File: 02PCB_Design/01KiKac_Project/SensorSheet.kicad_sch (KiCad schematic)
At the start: 10 parts, among them J1 MTSW-104-22-L-D-265-RA, U1 AS5047P-ATSM, U2 ISM330BXTR

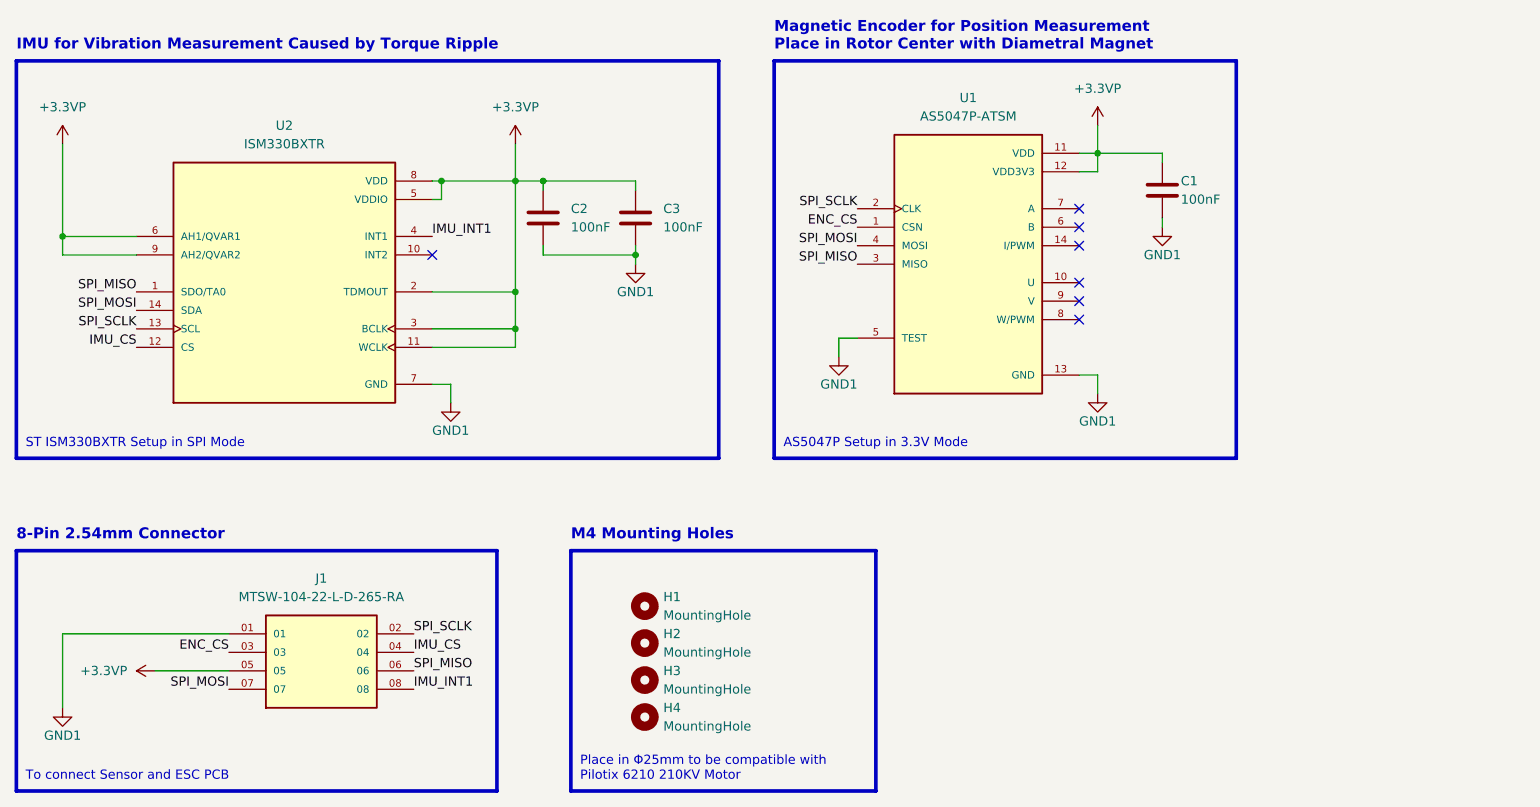
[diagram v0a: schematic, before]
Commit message: added CAN + minor changes
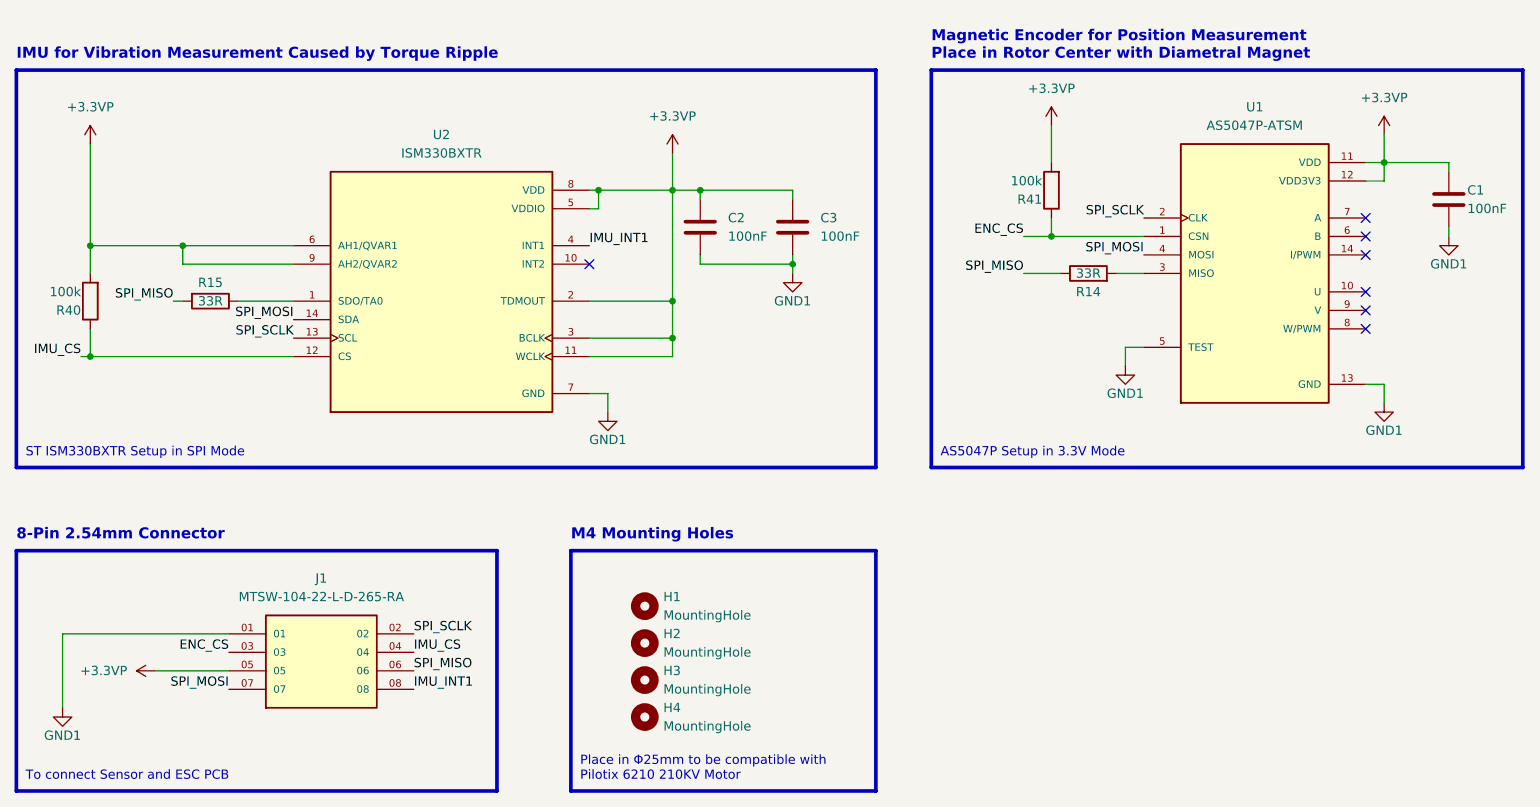
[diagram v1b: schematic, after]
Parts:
- added R14, R15: 33R, symbol Device:R
- added R40, R41: 100k, Resistor_SMD:R_0402_1005Metric_Pad0.72x0.64mm_HandSolder, symbol Device:R
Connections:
- net +3.3VP: now also R40.2, R41.2
- net ENC_CS: now also R41.1
- net IMU_CS: now also R40.1
- net SPI_MISO: now also R14.1, R15.2; no longer U1.3 (MISO), U2.1 (SDO/TA0)
- new net: R14.2, U1.3 (MISO)
- new net: R15.1, U2.1 (SDO/TA0)
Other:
- moved on the sheet: C1, C2, C3, U1, U2

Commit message: cleanup
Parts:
- renumbered R41 to R1, R14 to R2, R40 to R3, R15 to R4
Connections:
- net +3.3VP: now also R1.1; no longer R1.2
- net ENC_CS: now also R1.2; no longer R1.1
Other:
- moved on the sheet: R1, R2, R3, R4
